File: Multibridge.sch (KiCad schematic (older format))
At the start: 2 parts

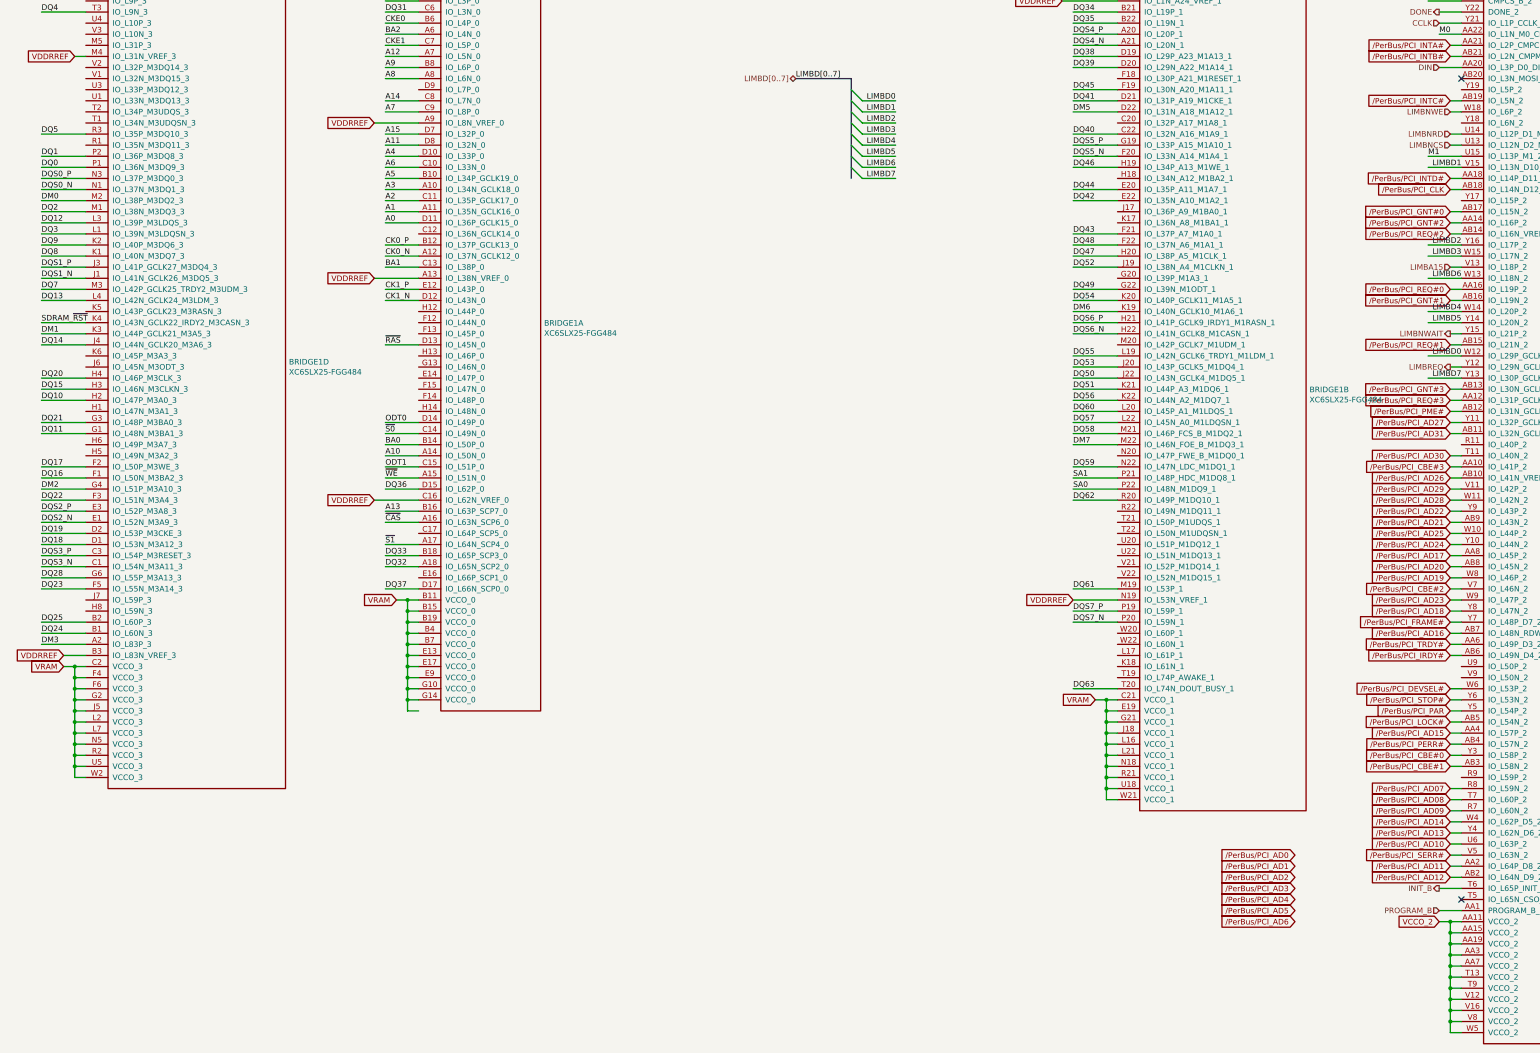
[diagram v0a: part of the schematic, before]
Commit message: Finish routing PCI
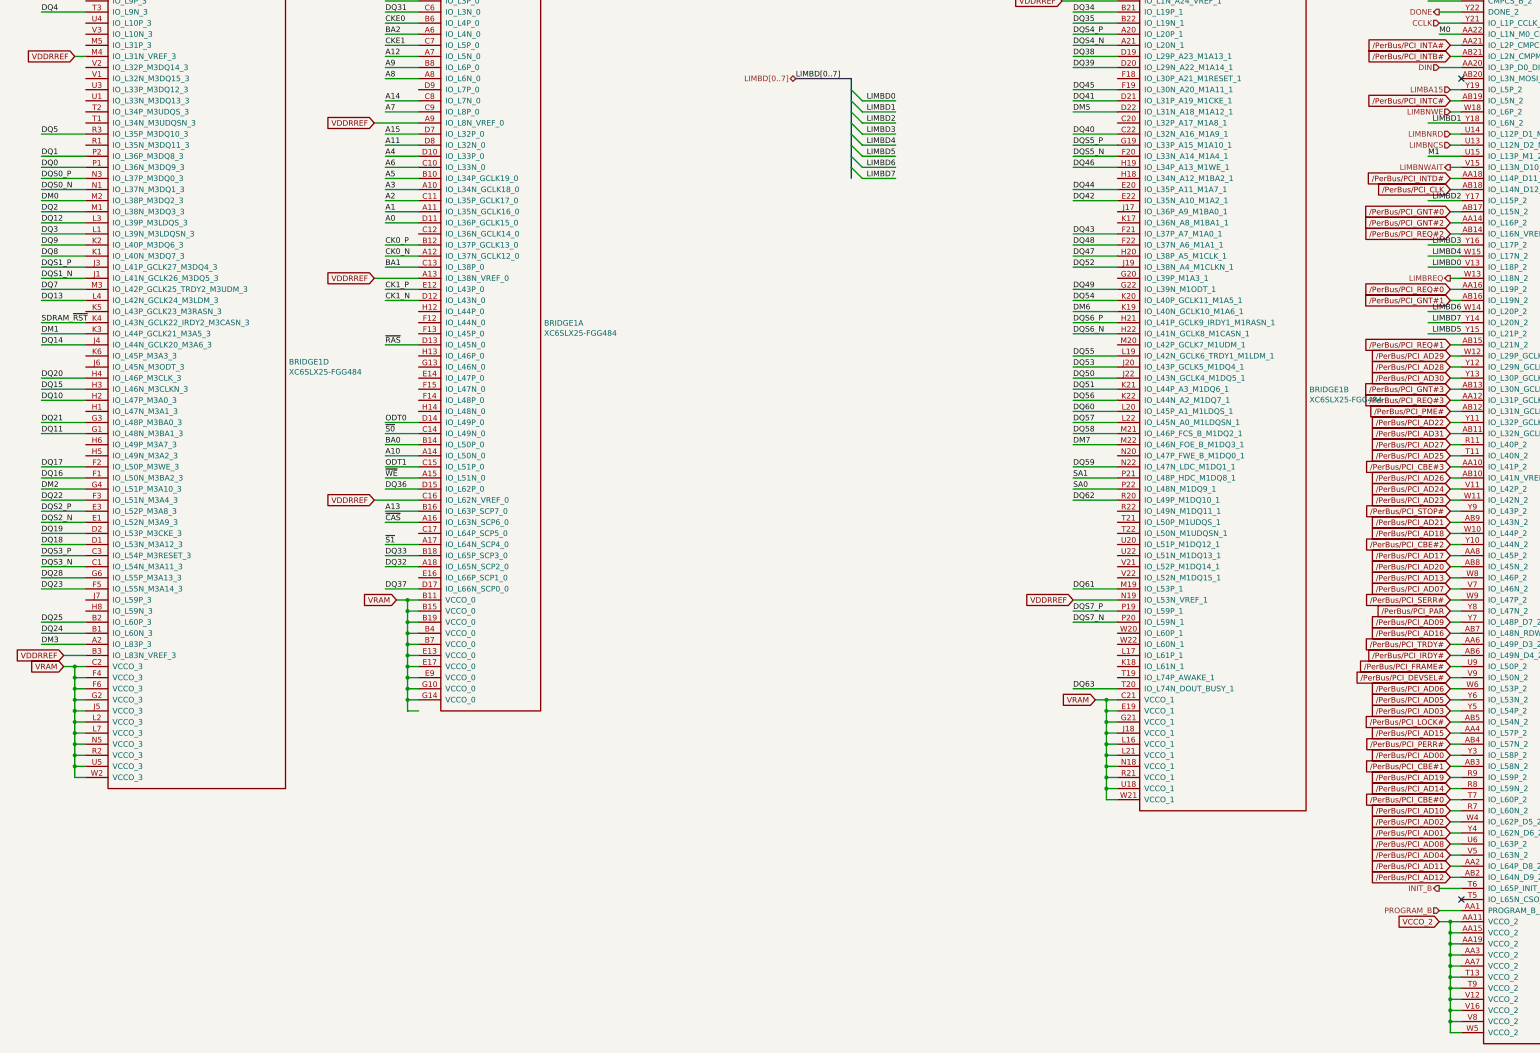
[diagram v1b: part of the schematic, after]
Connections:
- net labels added: /PerBus/PCI_AD00, /PerBus/PCI_AD01, /PerBus/PCI_AD02, /PerBus/PCI_AD03, /PerBus/PCI_AD04, /PerBus/PCI_AD05, /PerBus/PCI_AD06
- net labels removed: /PerBus/PCI_AD0, /PerBus/PCI_AD1, /PerBus/PCI_AD2, /PerBus/PCI_AD3, /PerBus/PCI_AD4, /PerBus/PCI_AD5, /PerBus/PCI_AD6
- wire segments 385 -> 431

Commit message: Break out CPU bus
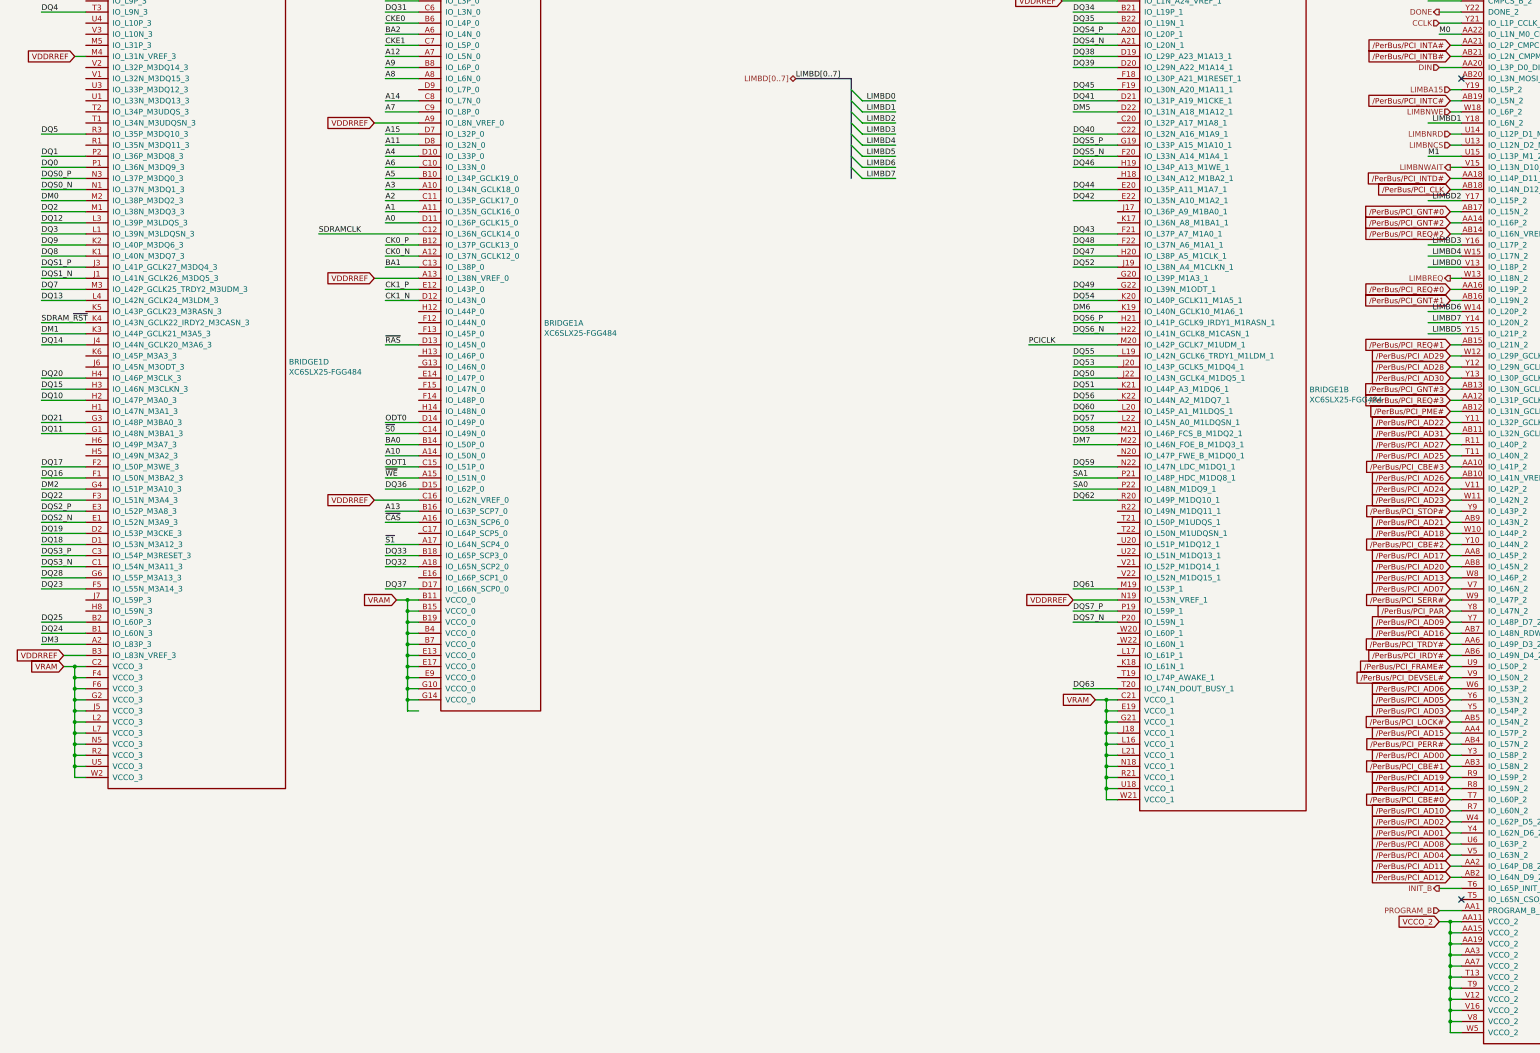
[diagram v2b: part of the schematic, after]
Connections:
- net labels added: PCICLK, SDRAMCLK
- wire segments 431 -> 394
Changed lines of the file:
@@
 	19600 8000 19000 8000
 Wire Wire Line
-	4700 7100 4800 7100
-Wire Wire Line
-	4800 7100 4900 7100
+	4700 7100 4900 7100
 Wire Wire Line
 	4800 7200 4900 7200
@@
 Connection ~ 4800 8000
 Wire Wire Line
-	4800 7100 4800 7200
-Wire Wire Line
-	4800 7200 4800 7300
-Wire Wire Line
-	4800 7300 4800 7400
-Wire Wire Line
-	4800 7400 4800 7500
-Wire Wire Line
-	4800 7500 4800 7600
-Wire Wire Line
-	4800 7600 4800 7700
-Wire Wire Line
-	4800 7700 4800 7800
-Wire Wire Line
-	4800 7800 4800 7900
-Wire Wire Line
-	4800 7900 4800 8000
-Wire Wire Line
-	4800 8000 4800 8100
+	4800 7100 4800 8100
 Wire Wire Line
 	1700 7600 1900 7600
@@
 	4500 6200 4900 6200
 Wire Wire Line
-	11000 8000 11100 8000
-Wire Wire Line
-	11100 8000 11200 8000
+	11000 8000 11200 8000
 Wire Wire Line
 	11100 8100 11200 8100
@@
 Connection ~ 11100 8800
 Wire Wire Line
-	11100 8000 11100 8100
-Wire Wire Line
-	11100 8100 11100 8200
-Wire Wire Line
-	11100 8200 11100 8300
-Wire Wire Line
-	11100 8300 11100 8400
-Wire Wire Line
-	11100 8400 11100 8500
-Wire Wire Line
-	11100 8500 11100 8600
-Wire Wire Line
-	11100 8600 11100 8700
-Wire Wire Line
-	11100 8700 11100 8800
-Wire Wire Line
-	11100 8800 11100 8900
+	11100 8000 11100 8900
 Connection ~ 11100 8000
 Wire Wire Line
@@
 Connection ~ 14200 10900
 Wire Wire Line
-	14200 10000 14200 10100
-Wire Wire Line
-	14200 10100 14200 10200
-Wire Wire Line
-	14200 10200 14200 10300
-Wire Wire Line
-	14200 10300 14200 10400
-Wire Wire Line
-	14200 10400 14200 10500
-Wire Wire Line
-	14200 10500 14200 10600
-Wire Wire Line
-	14200 10600 14200 10700
-Wire Wire Line
-	14200 10700 14200 10800
-Wire Wire Line
-	14200 10800 14200 10900
-Wire Wire Line
-	14200 10900 14200 11000
-Wire Wire Line
-	1700 7700 1800 7700
-Wire Wire Line
-	1800 7700 1900 7700
+	14200 10000 14200 11000
+Wire Wire Line
+	1700 7700 1900 7700
 Wire Wire Line
 	1800 7800 1900 7800
@@
 Connection ~ 1800 8600
 Wire Wire Line
-	1800 7700 1800 7800
-Wire Wire Line
-	1800 7800 1800 7900
-Wire Wire Line
-	1800 7900 1800 8000
-Wire Wire Line
-	1800 8000 1800 8100
-Wire Wire Line
-	1800 8100 1800 8200
-Wire Wire Line
-	1800 8200 1800 8300
-Wire Wire Line
-	1800 8300 1800 8400
-Wire Wire Line
-	1800 8400 1800 8500
-Wire Wire Line
-	1800 8500 1800 8600
-Wire Wire Line
-	1800 8600 1800 8700
+	1800 7700 1800 8700
 Wire Wire Line
 	8900 2600 9200 2600
@@
 	8900 3300 9200 3300
 Wire Bus Line
-	8800 2400 8800 2500
-Wire Bus Line
-	8800 2500 8800 2600
-Wire Bus Line
-	8800 2600 8800 2700
-Wire Bus Line
-	8800 2700 8800 2800
-Wire Bus Line
-	8800 2800 8800 2900
-Wire Bus Line
-	8800 2900 8800 3000
-Wire Bus Line
-	8800 3000 8800 3100
-Wire Bus Line
-	8800 3100 8800 3200
-Wire Bus Line
-	8800 3200 8800 3300
+	8800 2400 8800 3300
 Wire Bus Line
 	8800 2400 8300 2400
@@
 	14200 5400 14300 5400
 Wire Wire Line
-	14100 10000 14200 10000
-Wire Wire Line
-	14200 10000 14300 10000
+	14100 10000 14300 10000
 Wire Wire Line
 	14200 10100 14300 10100
@@
 Wire Wire Line
 	14200 7300 14300 7300
+Text Label 4000 3800 0    50   ~ 0
+SDRAMCLK
+Wire Wire Line
+	4900 3800 4000 3800
+Text Label 10400 4800 0    50   ~ 0
+PCICLK
+Wire Wire Line
+	10400 4800 11200 4800
 $EndSCHEMATC

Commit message: workworkwork
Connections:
- net labels added: CPU_ACK0#, CPU_ACK1#, CPU_ADDR#, CPU_CLK, CPU_D[0..31], CPU_INT0#, CPU_INT1#, CPU_REQ0#, CPU_REQ1#, CPU_WAIT#, CPU_WR#, PCI_AD0, PCI_AD1, PCI_AD10, PCI_AD11, PCI_AD12, PCI_AD13, PCI_AD14, PCI_AD15, PCI_AD16, PCI_AD17, PCI_AD18, PCI_AD19, PCI_AD2, PCI_AD20, PCI_AD21, PCI_AD22, PCI_AD23, PCI_AD24, PCI_AD25, PCI_AD26, PCI_AD27, PCI_AD28, PCI_AD29, PCI_AD3, PCI_AD30, PCI_AD31, PCI_AD4, PCI_AD5, PCI_AD6, PCI_AD7, PCI_AD8, PCI_AD9, PCI_AD[0..31], PCI_CLK, PCI_PAR, ~PCI_CBE0, ~PCI_CBE1, ~PCI_CBE2, ~PCI_CBE3, ~PCI_CBE[0..3], ~PCI_DEVSEL, ~PCI_FRAME, ~PCI_GNT0, ~PCI_GNT1, ~PCI_GNT2, ~PCI_GNT3, ~PCI_GNT[0..3], ~PCI_INT0, ~PCI_INT1, ~PCI_INT2, ~PCI_INT3, ~PCI_INT[0..3], ~PCI_IRDY, ~PCI_LOCK, ~PCI_PERR, ~PCI_REQ0, ~PCI_REQ1, ~PCI_REQ2, ~PCI_REQ3, ~PCI_REQ[0..3], ~PCI_SERR, ~PCI_STOP, ~PCI_TRDY
- net labels removed: /PerBus/PCI_AD00, /PerBus/PCI_AD01, /PerBus/PCI_AD02, /PerBus/PCI_AD03, /PerBus/PCI_AD04, /PerBus/PCI_AD05, /PerBus/PCI_AD06, /PerBus/PCI_AD07, /PerBus/PCI_AD08, /PerBus/PCI_AD09, /PerBus/PCI_AD10, /PerBus/PCI_AD11, /PerBus/PCI_AD12, /PerBus/PCI_AD13, /PerBus/PCI_AD14, /PerBus/PCI_AD15, /PerBus/PCI_AD16, /PerBus/PCI_AD17, /PerBus/PCI_AD18, /PerBus/PCI_AD19, /PerBus/PCI_AD20, /PerBus/PCI_AD21, /PerBus/PCI_AD22, /PerBus/PCI_AD23, /PerBus/PCI_AD24, /PerBus/PCI_AD25, /PerBus/PCI_AD26, /PerBus/PCI_AD27, /PerBus/PCI_AD28, /PerBus/PCI_AD29, /PerBus/PCI_AD30, /PerBus/PCI_AD31, /PerBus/PCI_CBE#0, /PerBus/PCI_CBE#1, /PerBus/PCI_CBE#2, /PerBus/PCI_CBE#3, /PerBus/PCI_CLK, /PerBus/PCI_DEVSEL#, /PerBus/PCI_FRAME#, /PerBus/PCI_GNT#0, /PerBus/PCI_GNT#1, /PerBus/PCI_GNT#2, /PerBus/PCI_GNT#3, /PerBus/PCI_INTA#, /PerBus/PCI_INTB#, /PerBus/PCI_INTC#, /PerBus/PCI_INTD#, /PerBus/PCI_IRDY#, /PerBus/PCI_LOCK#, /PerBus/PCI_PAR, /PerBus/PCI_PERR#, /PerBus/PCI_PME#, /PerBus/PCI_REQ#0, /PerBus/PCI_REQ#1, /PerBus/PCI_REQ#2, /PerBus/PCI_REQ#3, /PerBus/PCI_SERR#, /PerBus/PCI_STOP#, /PerBus/PCI_TRDY#
- wire segments 394 -> 393
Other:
- note added: "Free"
